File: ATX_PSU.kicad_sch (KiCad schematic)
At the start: 0 parts

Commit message: updated readme & initial setup
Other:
- title: ModuCard power supply unit -> ModuCard ATX power supply adapter
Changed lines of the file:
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@@
 	(paper "A4")
 	(title_block
-		(title "ModuCard power supply unit")
+		(title "ModuCard ATX power supply adapter")
 		(date "2025-08-05")
 		(rev "0")
@@
 		(comment 1 "Base project authors: Dominik Pluta, Artem Horiunov")
 		(comment 2 "Project author: Maciej Chodowiec")
+		(comment 3 "Fork author: Wojciech Szafrański")
 	)
 	(bus_alias "CAN"
@@
 		)
 		(instances
-			(project "PSU"
+			(project "ATX_PSU"
 				(path "/090a8e41-87a8-4fb1-998b-60a2c0dc4cee"
 					(page "6")
@@
 		)
 		(instances
-			(project "PSU"
+			(project "ATX_PSU"
 				(path "/090a8e41-87a8-4fb1-998b-60a2c0dc4cee"
 					(page "12")
@@
 		)
 		(instances
-			(project "PSU"
+			(project "ATX_PSU"
 				(path "/090a8e41-87a8-4fb1-998b-60a2c0dc4cee"
 					(page "3")
@@
 		)
 		(instances
-			(project "PSU"
+			(project "ATX_PSU"
 				(path "/090a8e41-87a8-4fb1-998b-60a2c0dc4cee"
 					(page "5")
@@
 		)
 		(instances
-			(project "PSU"
+			(project "ATX_PSU"
 				(path "/090a8e41-87a8-4fb1-998b-60a2c0dc4cee"
 					(page "14")
@@
 		)
 		(instances
-			(project "PSU"
+			(project "ATX_PSU"
 				(path "/090a8e41-87a8-4fb1-998b-60a2c0dc4cee"
 					(page "8")
@@
 		)
 		(instances
-			(project "PSU"
+			(project "ATX_PSU"
 				(path "/090a8e41-87a8-4fb1-998b-60a2c0dc4cee"
 					(page "4")
@@
 		)
 		(instances
-			(project "PSU"
+			(project "ATX_PSU"
 				(path "/090a8e41-87a8-4fb1-998b-60a2c0dc4cee"
 					(page "9")
@@
 		)
 		(instances
-			(project "PSU"
+			(project "ATX_PSU"
 				(path "/090a8e41-87a8-4fb1-998b-60a2c0dc4cee"
 					(page "11")
@@
 		)
 		(instances
-			(project "PSU"
+			(project "ATX_PSU"
 				(path "/090a8e41-87a8-4fb1-998b-60a2c0dc4cee"
 					(page "13")
@@
 		)
 		(instances
-			(project "PSU"
+			(project "ATX_PSU"
 				(path "/090a8e41-87a8-4fb1-998b-60a2c0dc4cee"
 					(page "10")
@@
 		)
 		(instances
-			(project "PSU"
+			(project "ATX_PSU"
 				(path "/090a8e41-87a8-4fb1-998b-60a2c0dc4cee"
 					(page "7")
@@
 		)
 		(instances
-			(project "PSU"
+			(project "ATX_PSU"
 				(path "/090a8e41-87a8-4fb1-998b-60a2c0dc4cee"
 					(page "2")

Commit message: most changes done
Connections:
- no-connect marks 3 -> 2
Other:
- added sheet ATX connector (ATX connector.kicad_sch)
- added sheet Power_switch (Power_switch.kicad_sch)
- sheet MCU ports: added MCU_ATX_ON, PWR_OK; removed ADS1115/RDY, MASTER_ON, PowerButton
- note added: "TO DO Calculate LED resistor Why max current for current sense I2C addreses 24V Converter"

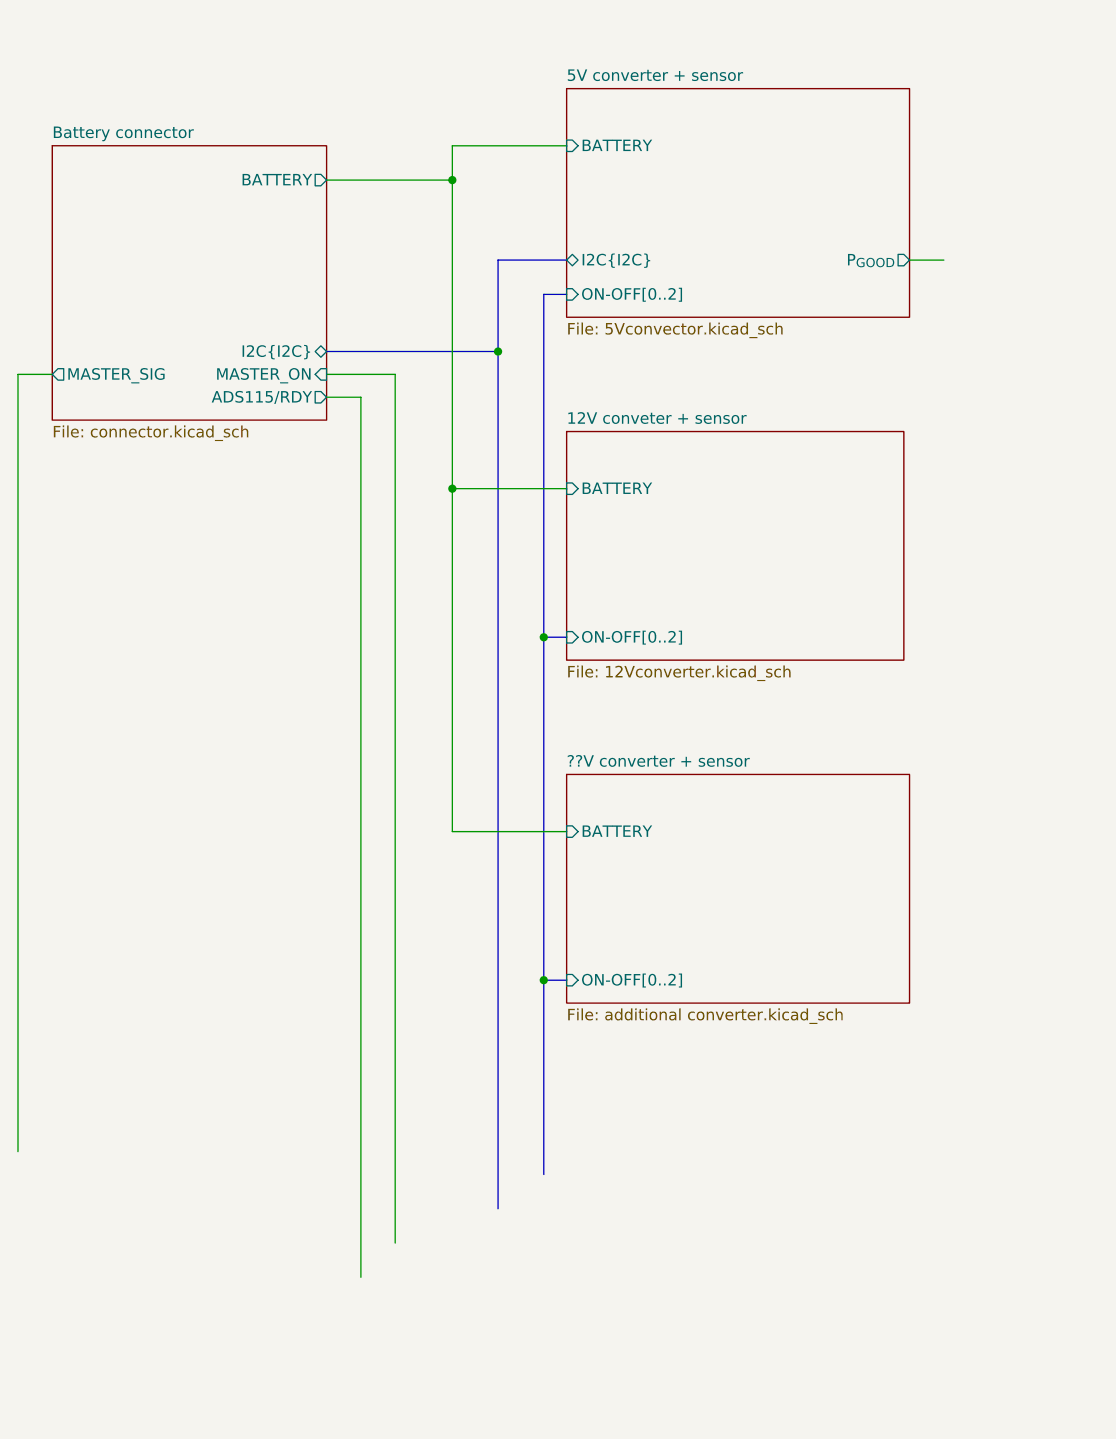
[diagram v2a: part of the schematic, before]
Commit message: removed not needed sheets
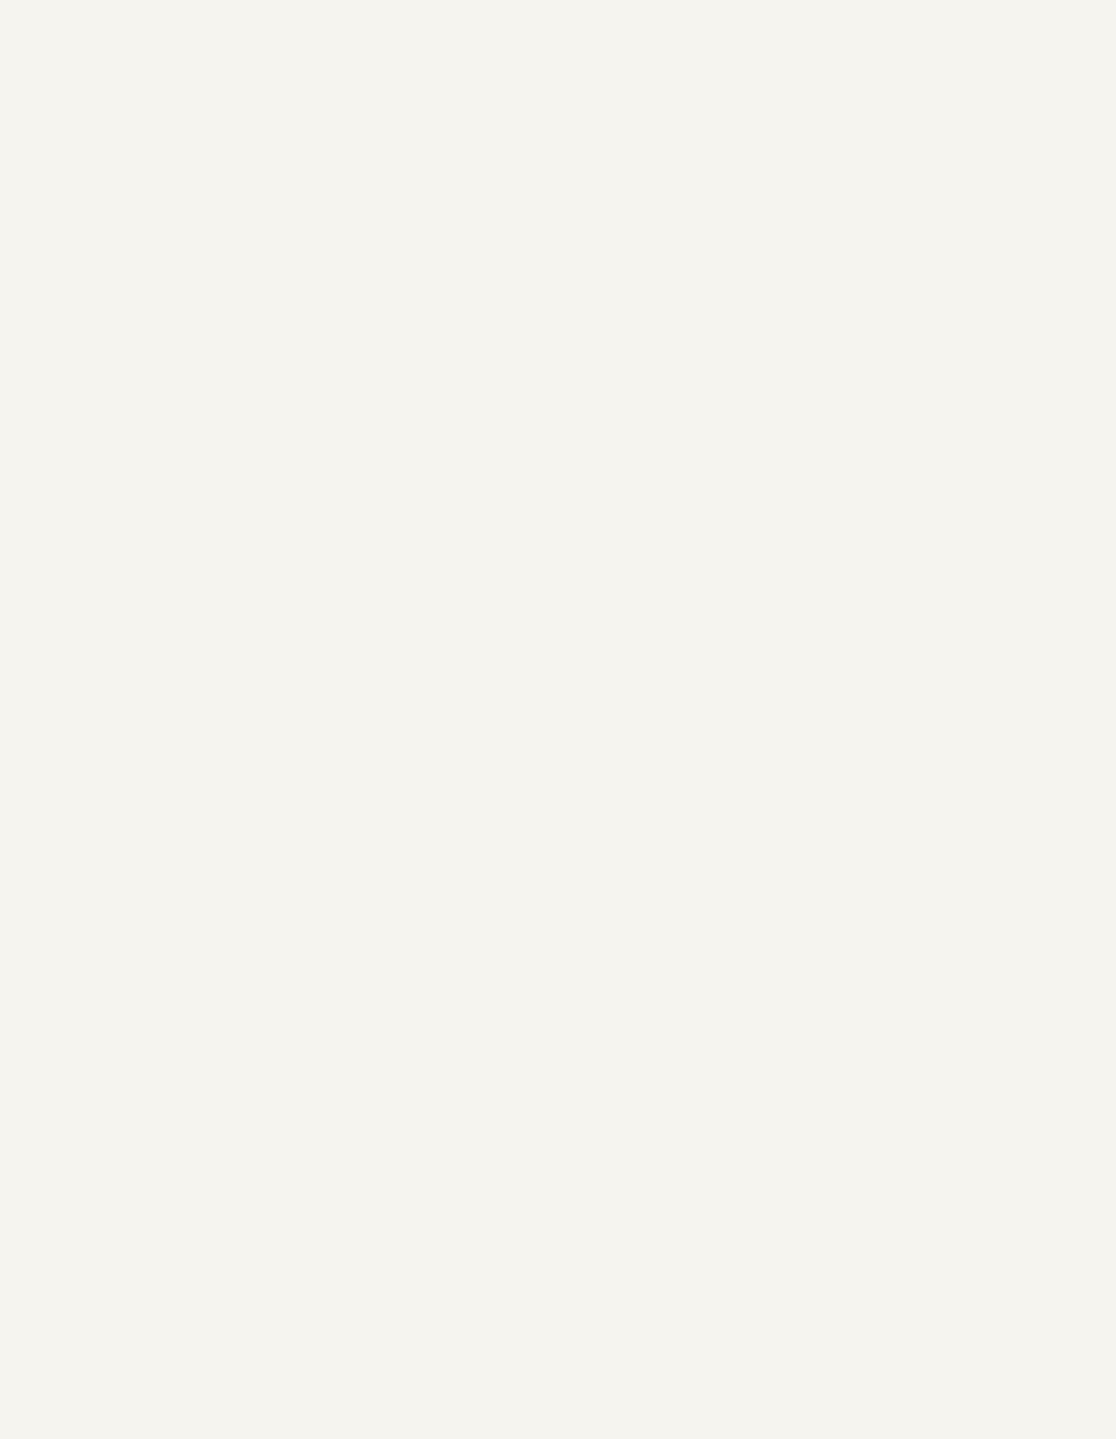
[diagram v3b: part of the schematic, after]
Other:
- removed sheet 12V conveter + sensor
- removed sheet 5V converter + sensor
- removed sheet ??V converter + sensor
- removed sheet Battery connector

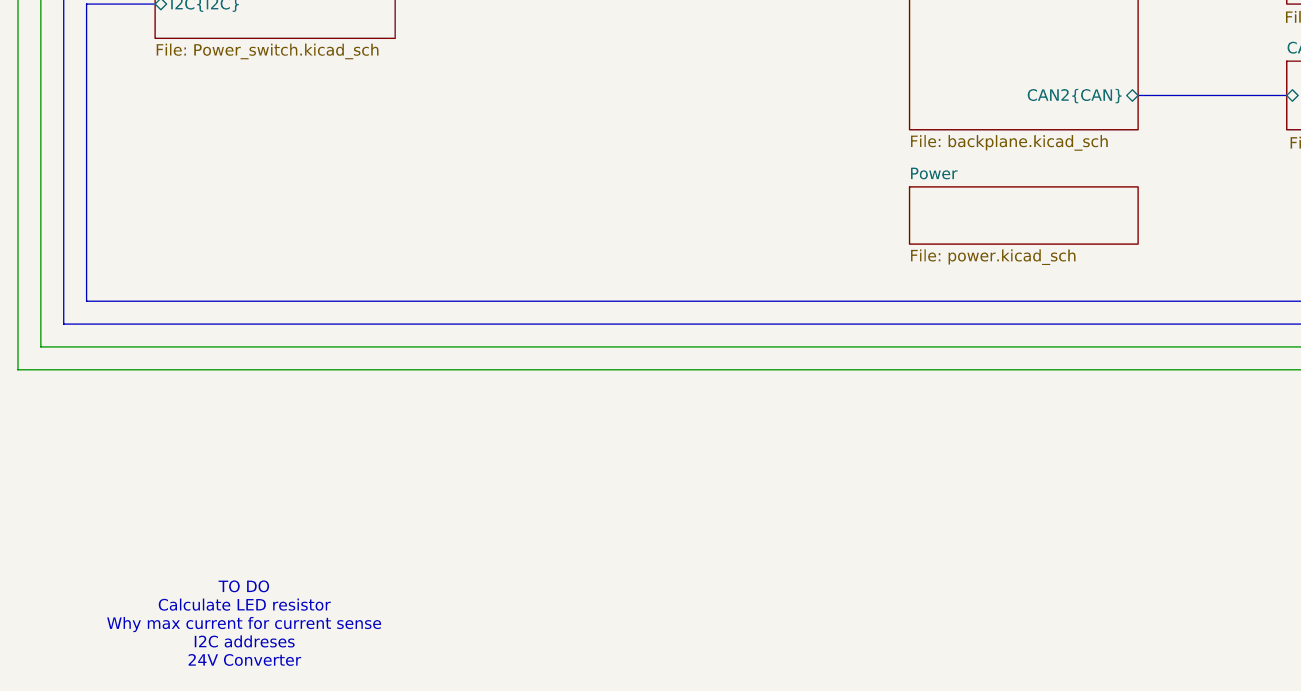
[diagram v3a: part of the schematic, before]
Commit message: removed 3V3 converter
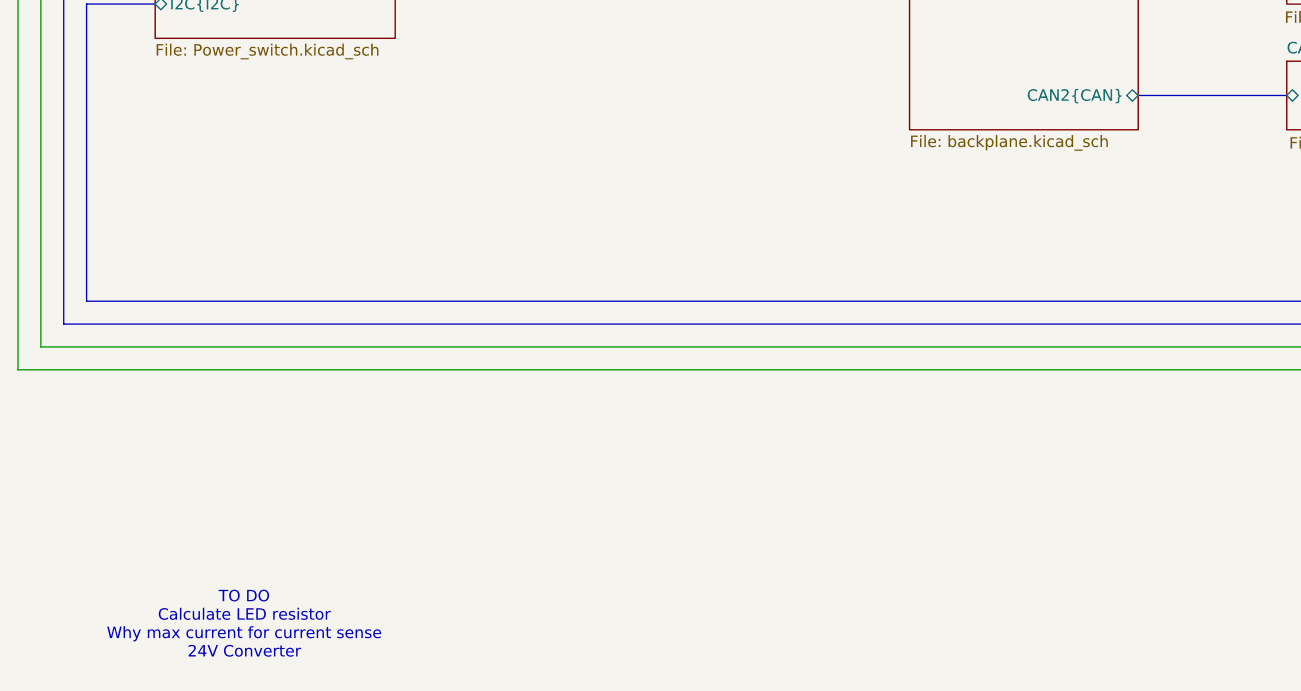
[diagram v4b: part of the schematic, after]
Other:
- removed sheet Power
- note added: "TO DO Calculate LED resistor Why max current for current sense 24V Converter"
- note removed: "TO DO Calculate LED resistor Why max current for current sense I2C addreses 24V Converter"
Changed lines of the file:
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@@
 		(members "+" "-")
 	)
-	(text "TO DO\nCalculate LED resistor\nWhy max current for current sense\nI2C addreses\n24V Converter"
+	(text "TO DO\nCalculate LED resistor\nWhy max current for current sense\n24V Converter"
 		(exclude_from_sim no)
 		(at 59.436 179.578 0)
@@
 				)
 			)
-		)
-	)
-	(sheet
-		(at 133.35 130.81)
-		(size 25.4 6.35)
-		(exclude_from_sim no)
-		(in_bom yes)
-		(on_board yes)
-		(dnp no)
-		(fields_autoplaced yes)
-		(stroke
-			(width 0.1524)
-			(type solid)
-		)
-		(fill
-			(color 0 0 0 0.0000)
-		)
-		(property "Sheetname" "Power"
-			(at 133.35 130.0984 0)
-			(effects
-				(font
-					(size 1.27 1.27)
-				)
-				(justify left bottom)
-			)
-		)
-		(property "Sheetfile" "power.kicad_sch"
-			(at 133.35 137.7446 0)
-			(effects
-				(font
-					(size 1.27 1.27)
-				)
-				(justify left top)
-			)
-		)
-		(instances
-			(project "ATX_PSU"
-				(path "/090a8e41-87a8-4fb1-998b-60a2c0dc4cee"
-					(page "3")
-				)
-			)

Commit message: routing progress
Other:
- sheet ATX connector ports: added ATX{ATX}, PWR_OK_ATX; removed ATX, PWR_OK
- sheet Power_switch ports: added ATX{ATX}; removed ATX
- note added: "TO DO Calculate LED resistor Why max current for current sense 24V Converter add temp sensing"
- note removed: "TO DO Calculate LED resistor Why max current for current sense 24V Converter"
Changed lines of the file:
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@@
 		(members "+" "-")
 	)
-	(text "TO DO\nCalculate LED resistor\nWhy max current for current sense\n24V Converter"
+	(text "TO DO\nCalculate LED resistor\nWhy max current for current sense\n24V Converter\nadd temp sensing"
 		(exclude_from_sim no)
 		(at 59.436 179.578 0)
@@
 		)
 	)
+	(bus
+		(pts
+			(xy 82.55 97.79) (xy 76.2 97.79)
+		)
+		(stroke
+			(width 0)
+			(type default)
+		)
+	)
+	(bus
+		(pts
+			(xy 76.2 72.39) (xy 82.55 72.39)
+		)
+		(stroke
+			(width 0)
+			(type default)
+		)
+	)
 	(wire
 		(pts
@@
 		)
 	)
+	(bus
+		(pts
+			(xy 82.55 72.39) (xy 82.55 97.79)
+		)
+		(stroke
+			(width 0)
+			(type default)
+		)
+	)
 	(wire
 		(pts
@@
 	(bus
 		(pts
-			(xy 83.82 72.39) (xy 76.2 72.39)
-		)
-		(stroke
-			(width 0)
-			(type default)
-		)
-	)
-	(bus
-		(pts
 			(xy 39.37 107.95) (xy 39.37 146.05)
 		)
@@
 	(bus
 		(pts
-			(xy 76.2 97.79) (xy 83.82 97.79)
-		)
-		(stroke
-			(width 0)
-			(type default)
-		)
-	)
-	(bus
-		(pts
 			(xy 200.66 106.68) (xy 213.36 106.68)
 		)
@@
 		(pts
 			(xy 168.91 60.96) (xy 168.91 76.2)
-		)
-		(stroke
-			(width 0)
-			(type default)
-		)
-	)
-	(bus
-		(pts
-			(xy 83.82 97.79) (xy 83.82 72.39)
 		)
 		(stroke
@@
 			)
 		)
-		(pin "ATX" input
+		(pin "ATX{ATX}" input
 			(at 76.2 97.79 0)
 			(effects
@@
 			)
 		)
-		(pin "ATX" output
+		(pin "PWR_OK_ATX" output
+			(at 49.53 64.77 180)
+			(effects
+				(font
+					(size 1.27 1.27)
+				)
+				(justify left)
+			)
+		)
+		(pin "ATX{ATX}" output
 			(at 76.2 72.39 0)
 			(effects
@@
 			)
 		)
-		(pin "PWR_OK" output
-			(at 49.53 64.77 180)
-			(effects
-				(font
-					(size 1.27 1.27)
-				)
-				(justify left)
-			)
-		)

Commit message: finished routing
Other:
- note added: "TO DO Calculate LED resistor"
- note removed: "TO DO Calculate LED resistor Why max current for current sense 24V Converter add temp sensing"
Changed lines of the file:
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@@
 		(members "+" "-")
 	)
-	(text "TO DO\nCalculate LED resistor\nWhy max current for current sense\n24V Converter\nadd temp sensing"
+	(text "TO DO\nCalculate LED resistor\n"
 		(exclude_from_sim no)
 		(at 59.436 179.578 0)

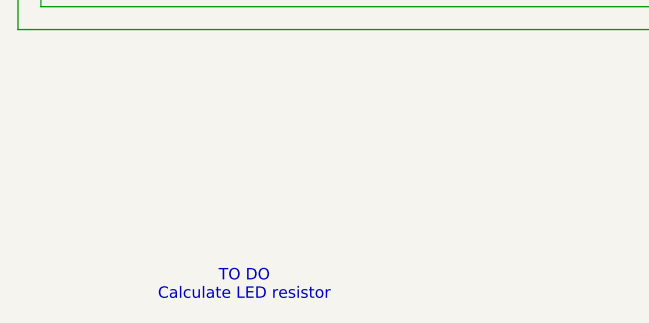
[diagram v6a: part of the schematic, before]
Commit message: updated LED resistor values
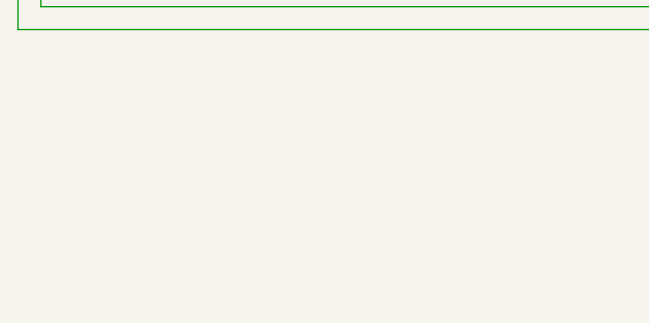
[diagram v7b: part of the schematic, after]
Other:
- note removed: "TO DO Calculate LED resistor"
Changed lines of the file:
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@@
 		(members "+" "-")
-	)
-	(text "TO DO\nCalculate LED resistor\n"
-		(exclude_from_sim no)
-		(at 59.436 179.578 0)
-		(effects
-			(font
-				(size 1.27 1.27)
-			)
-		)
 	)
 	(no_connect
